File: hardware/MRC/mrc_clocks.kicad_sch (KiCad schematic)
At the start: 8 parts, among them U3 XLH736120.000000I, U7 LMK1D1204P

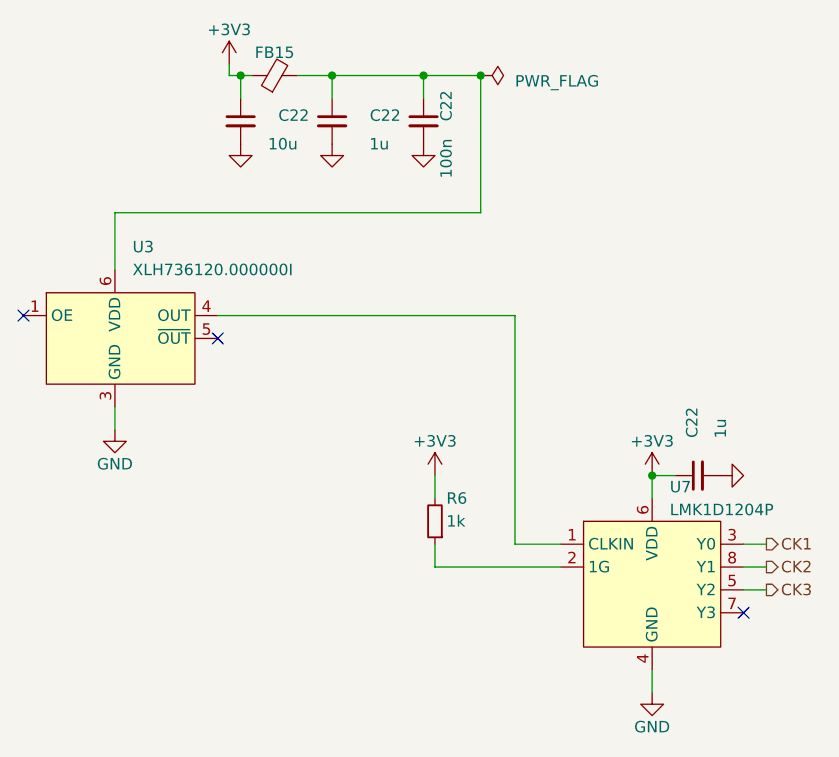
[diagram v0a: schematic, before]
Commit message: Update KiCAD Version, Integrate Libraries
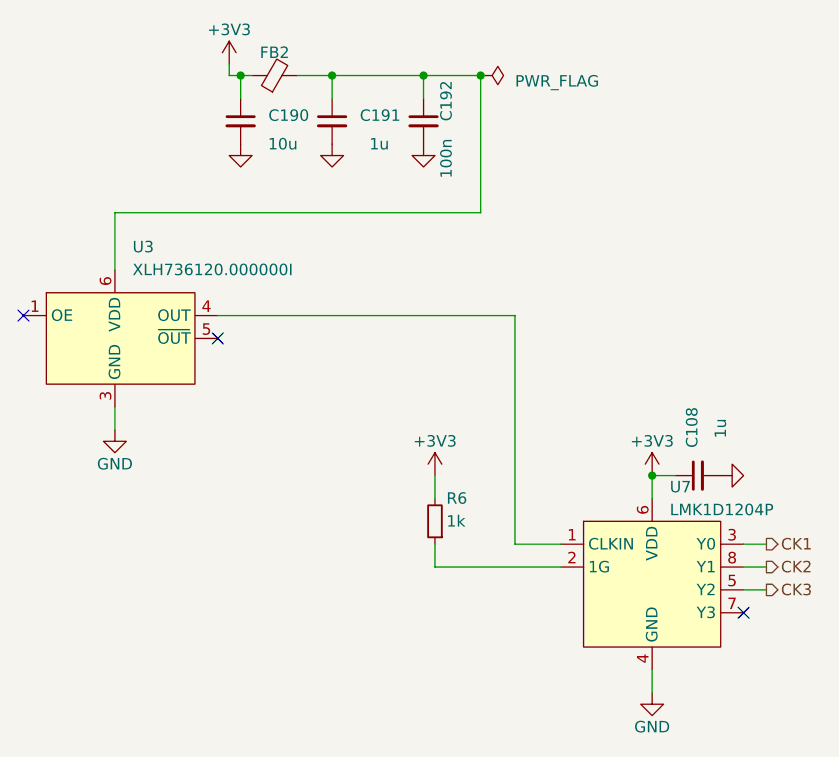
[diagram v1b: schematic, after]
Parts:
- U3: value XLH736120.000000I -> XLH736120.000000I
- renumbered C22 to C108, C22 to C190, C22 to C191, C22 to C192, FB15 to FB2

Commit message: Clean bill of materials
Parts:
- C108, C191: MPN (none) -> KGM15BR51E105KM
- C190: MPN (none) -> KGM15CR51A106MT
- C192: MPN (none) -> C0603C104K1RACAUTO
- FB2: MPN (none) -> 742792641
- R6: MPN (none) -> CRCW06031K00DHEBP
- U3: MPN (none) -> XLH736120.000000I
- U7: MPN (none) -> LMK1D1204PRHDR
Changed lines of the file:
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@@
+			)
+		)
+		(property "MPN" "CRCW06031K00DHEBP "
+			(at 119.38 105.41 0)
+			(effects
+				(font
+					(size 1.27 1.27)
+				)
+				(hide yes)
 			)
 		)
@@
 			)
 		)
+		(property "MPN" "KGM15CR51A106MT "
+			(at 97.79 60.96 0)
+			(effects
+				(font
+					(size 1.27 1.27)
+				)
+				(hide yes)
+			)
+		)
 		(pin "1"
 		)
@@
 			)
 		)
+		(property "MPN" "742792641 "
+			(at 101.6 55.88 90)
+			(effects
+				(font
+					(size 1.27 1.27)
+				)
+				(hide yes)
+			)
+		)
 		(pin "1"
 		)
@@
 			)
 		)
+		(property "MPN" "KGM15BR51E105KM "
+			(at 107.95 60.96 0)
+			(effects
+				(font
+					(size 1.27 1.27)
+				)
+				(hide yes)
+			)
+		)
 		(pin "1"
 		)
@@
 			)
 		)
+		(property "MPN" "KGM15BR51E105KM "
+			(at 148.59 100.33 0)
+			(effects
+				(font
+					(size 1.27 1.27)
+				)
+				(hide yes)
+			)
+		)
 		(pin "1"
 		)
@@
 			)
 		)
+		(property "MPN" "LMK1D1204PRHDR "
+			(at 143.51 111.76 0)
+			(effects
+				(font
+					(size 1.27 1.27)
+				)
+				(hide yes)
+			)
+		)
 		(pin "1"
 		)
@@
 			)
 		)
+		(property "MPN" "XLH736120.000000I"
+			(at 83.82 85.09 0)
+			(effects
+				(font
+					(size 1.27 1.27)
+				)
+				(hide yes)
+			)
+		)
 		(pin "1"
 		)
@@
 			)
 		)
+		(property "MPN" "C0603C104K1RACAUTO "
+			(at 118.11 60.96 90)
+			(effects
+				(font
+					(size 1.27 1.27)
+				)
+				(hide yes)
+			)
+		)
